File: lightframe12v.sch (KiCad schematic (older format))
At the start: 47 parts, among them J1 PJ-077, J2 Conn_01x07_Female, J4 Conn_01x07_Female, J5 Conn_01x04_Female, J6 Conn_01x4_Female, Q1 MMBT2222A-TP, Q2 MMBT2222A-TP, SW1 SW_Push, SW2 SW_Push, U1 TPS562211, U2 ESP32-WROOM-32U, U3 TLC5971

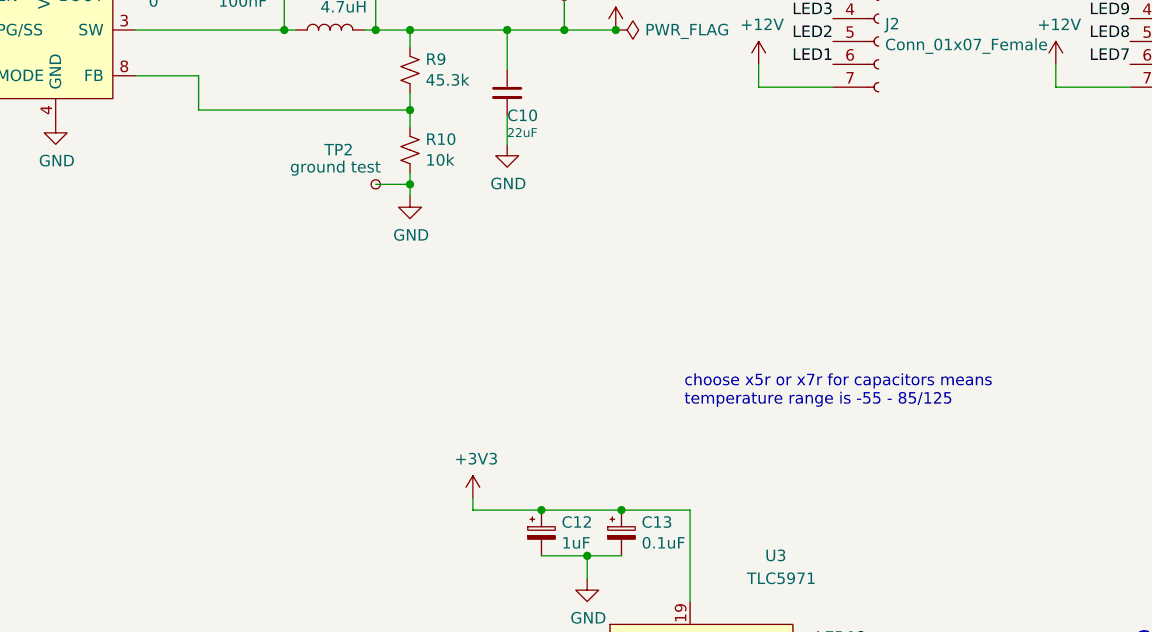
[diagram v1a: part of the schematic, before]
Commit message: Fiducials and mount points.
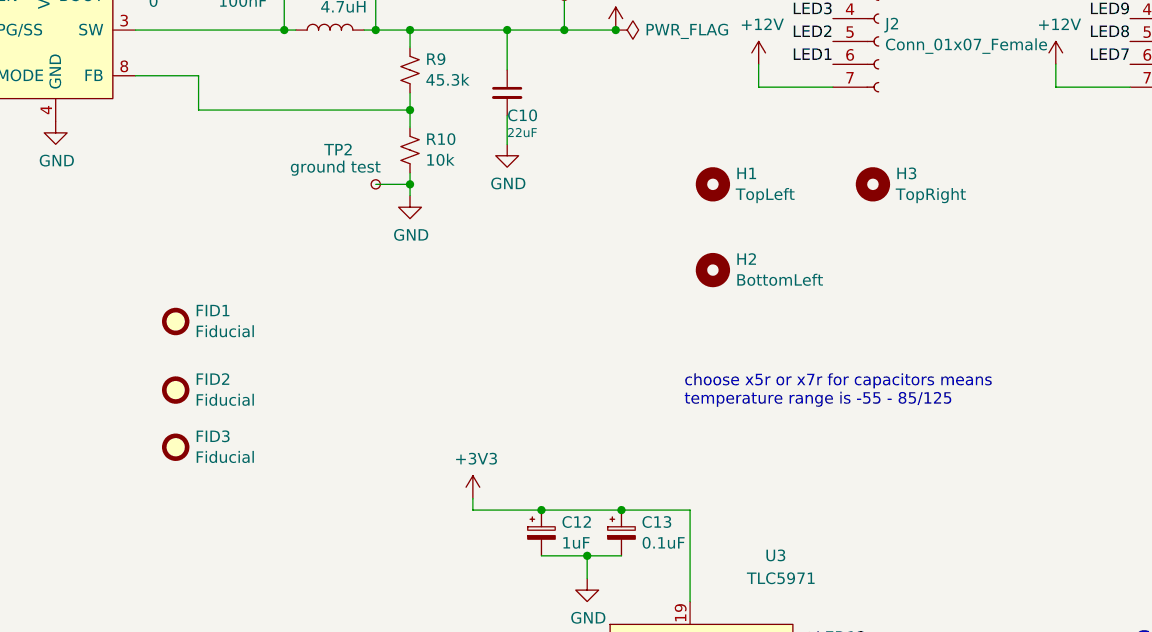
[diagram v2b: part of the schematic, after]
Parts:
- added FID1, FID2, FID3: Fiducial, Fiducial:Fiducial_1mm_Mask2mm, symbol Mechanical:Fiducial
- added H1: TopLeft, MountingHole:MountingHole_2.2mm_M2, symbol Mechanical:MountingHole
- added H2: BottomLeft, MountingHole:MountingHole_2.2mm_M2, symbol Mechanical:MountingHole
- added H3: TopRight, MountingHole:MountingHole_2.2mm_M2, symbol Mechanical:MountingHole
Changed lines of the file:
@@
+	1    0    0    -1
+$EndComp
+$Comp
+L Mechanical:MountingHole H3
+U 1 1 60715E68
+P 8550 2250
+F 0 "H3" H 8650 2296 50  0000 L CNN
+F 1 "TopRight" H 8650 2205 50  0000 L CNN
+F 2 "MountingHole:MountingHole_2.2mm_M2" H 8550 2250 50  0001 C CNN
+F 3 "~" H 8550 2250 50  0001 C CNN
+	1    8550 2250
+	1    0    0    -1
+$EndComp
+$Comp
+L Mechanical:MountingHole H1
+U 1 1 6071CBF1
+P 7850 2250
+F 0 "H1" H 7950 2296 50  0000 L CNN
+F 1 "TopLeft" H 7950 2205 50  0000 L CNN
+F 2 "MountingHole:MountingHole_2.2mm_M2" H 7850 2250 50  0001 C CNN
+F 3 "~" H 7850 2250 50  0001 C CNN
+	1    7850 2250
+	1    0    0    -1
+$EndComp
+$Comp
+L Mechanical:MountingHole H2
+U 1 1 607216A9
+P 7850 2625
+F 0 "H2" H 7950 2671 50  0000 L CNN
+F 1 "BottomLeft" H 7950 2580 50  0000 L CNN
+F 2 "MountingHole:MountingHole_2.2mm_M2" H 7850 2625 50  0001 C CNN
+F 3 "~" H 7850 2625 50  0001 C CNN
+	1    7850 2625
+	1    0    0    -1
+$EndComp
+$Comp
+L Mechanical:Fiducial FID1
+U 1 1 60726C05
+P 5500 2850
+F 0 "FID1" H 5585 2896 50  0000 L CNN
+F 1 "Fiducial" H 5585 2805 50  0000 L CNN
+F 2 "Fiducial:Fiducial_1mm_Mask2mm" H 5500 2850 50  0001 C CNN
+F 3 "~" H 5500 2850 50  0001 C CNN
+	1    5500 2850
+	1    0    0    -1
+$EndComp
+$Comp
+L Mechanical:Fiducial FID2
+U 1 1 60727705
+P 5500 3150
+F 0 "FID2" H 5585 3196 50  0000 L CNN
+F 1 "Fiducial" H 5585 3105 50  0000 L CNN
+F 2 "Fiducial:Fiducial_1mm_Mask2mm" H 5500 3150 50  0001 C CNN
+F 3 "~" H 5500 3150 50  0001 C CNN
+	1    5500 3150
+	1    0    0    -1
+$EndComp
+$Comp
+L Mechanical:Fiducial FID3
+U 1 1 6072BFCF
+P 5500 3400
+F 0 "FID3" H 5585 3446 50  0000 L CNN
+F 1 "Fiducial" H 5585 3355 50  0000 L CNN
+F 2 "Fiducial:Fiducial_1mm_Mask2mm" H 5500 3400 50  0001 C CNN
+F 3 "~" H 5500 3400 50  0001 C CNN
+	1    5500 3400
 	1    0    0    -1
 $EndComp

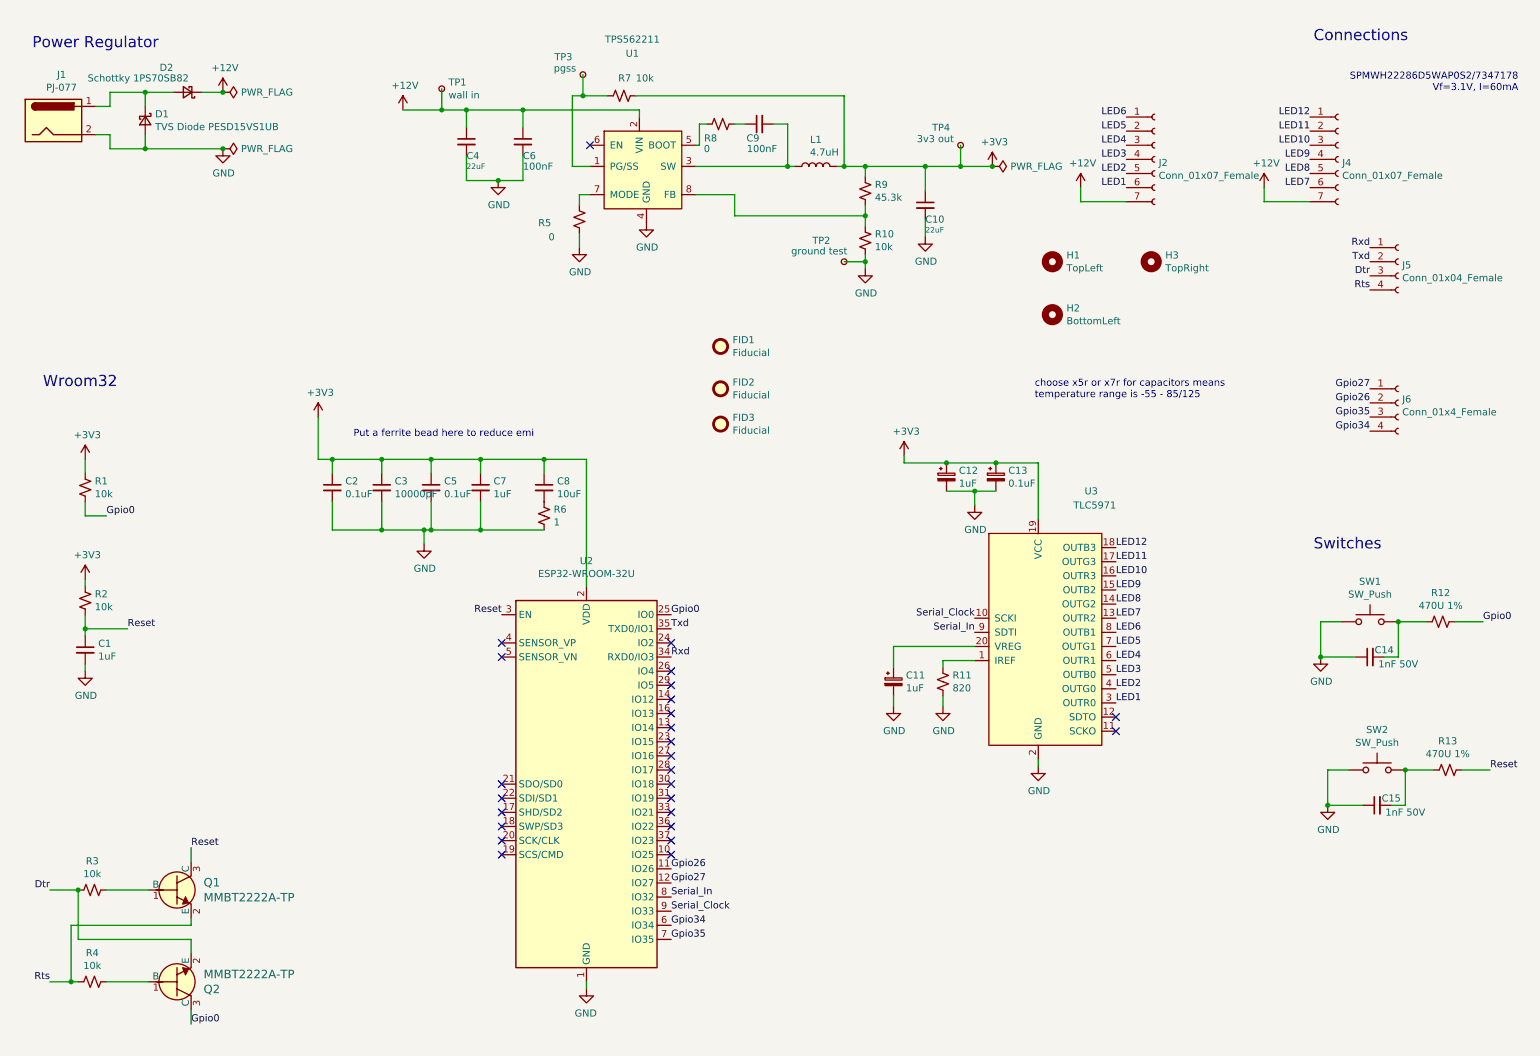
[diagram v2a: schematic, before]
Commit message: changes inductor footprint.
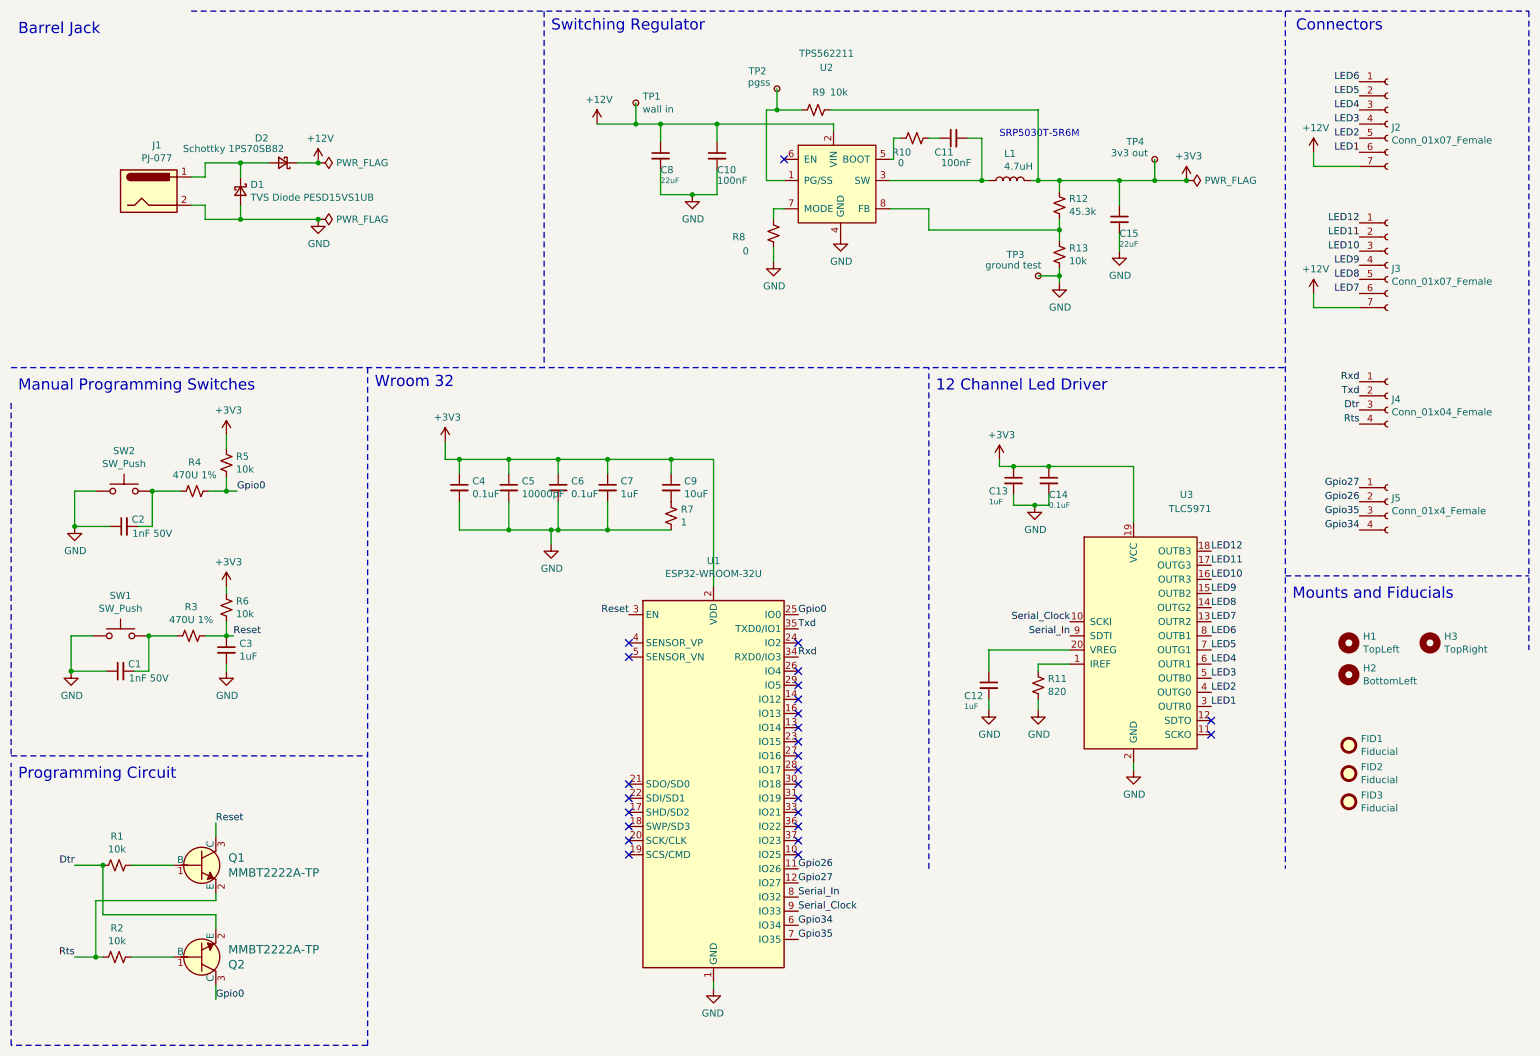
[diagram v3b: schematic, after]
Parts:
- removed C11, C12: 1uF, digikey-footprints:0603, symbol Device:CP_Small
- removed C13: 0.1uF, digikey-footprints:0603, symbol Device:CP_Small
- added C12, C13: 1uF, digikey-footprints:0603, symbol Device:C_Small
- added C14: 0.1uF, digikey-footprints:0603, symbol Device:C_Small
- L1: footprint Keith:SRN8040 Bournes -> Keith:SRP5030T-5R6M
- renumbered C15 to C1, C6 to C10, C9 to C11, C10 to C15, C14 to C2, C1 to C3, C2 to C4, C3 to C5, C5 to C6, C4 to C8, C8 to C9, J4 to J3, J5 to J4, J6 to J5, R3 to R1, R8 to R10, R9 to R12, R10 to R13, R4 to R2, R13 to R3, R12 to R4, R1 to R5, R2 to R6, R6 to R7, R5 to R8, R7 to R9, SW2 to SW1, SW1 to SW2, TP3 to TP2, TP2 to TP3, U2 to U1, U1 to U2
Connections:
- net +3V3: now also C13.1, C14.1
- net GND: now also C12.2, C13.2, C14.2
- net at U3.20 (VREG): now also C12.1
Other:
- note added: "12 Channel Led Driver"
- note added: "Barrel Jack"
- note added: "Connectors"
- note added: "Manual Programming Switches"
- note added: "Mounts and Fiducials\n"
- note added: "Programming Circuit"
- note added: "SRP5030T-5R6M"
- note added: "Switching Regulator"
- note added: "Wroom 32"
- note removed: "Connections"
- note removed: "Power Regulator"
- note removed: "Put a ferrite bead here to reduce emi"
- note removed: "SPMWH22286D5WAP0S2/7347178\nVf=3.1V, I=60mA"
- note removed: "Switches"
- note removed: "Wroom32"
- note removed: "choose x5r or x7r for capacitors means \ntemperature range is -55 - 85/125"
- moved on the sheet: C1, C10, C11, C15, C2, C3, C4, C5, C6, C7, C8, C9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

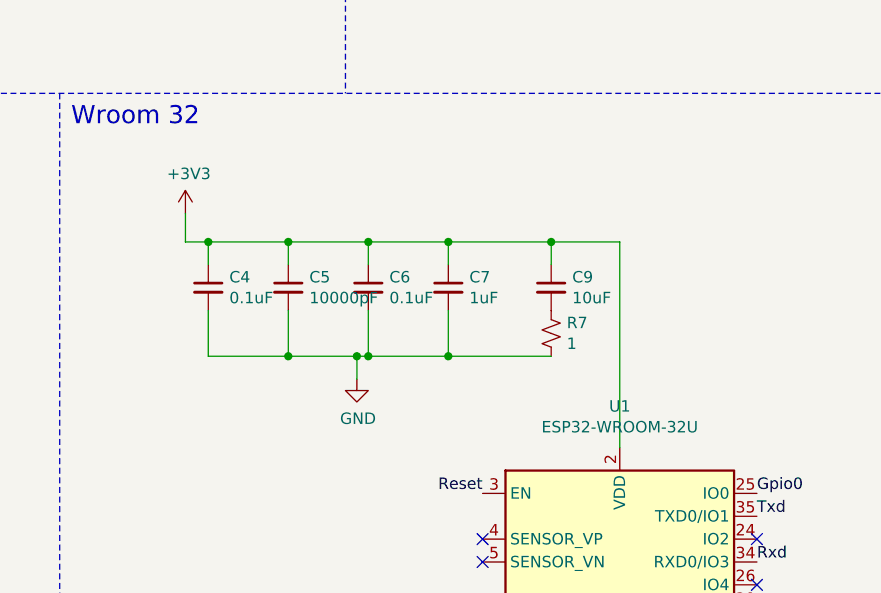
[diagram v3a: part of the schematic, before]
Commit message: Reduced decoupling and increased traces.
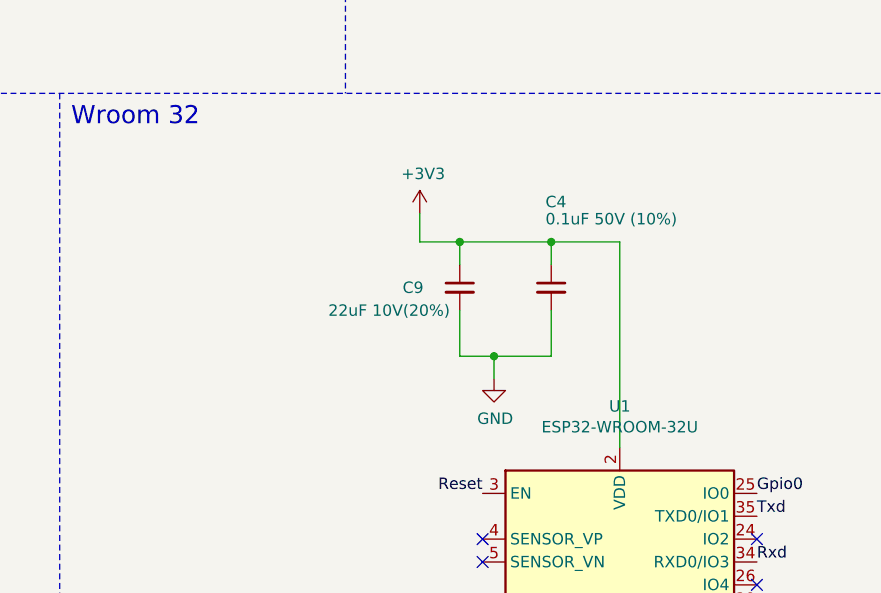
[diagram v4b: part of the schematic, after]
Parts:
- removed C5: 10000pF, digikey-footprints:0603, symbol Device:C_Small
- removed C6: 0.1uF, digikey-footprints:0603, symbol Device:C_Small
- removed C7: 1uF, digikey-footprints:0603, symbol Device:C_Small
- removed R7: 1, Resistor_SMD:R_0402_1005Metric, symbol Device:R_Small_US
- C4: value 0.1uF -> 0.1uF 50V (10%)
- C9: value 10uF -> 22uF 10V(20%)
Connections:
- net GND: now also C9.2
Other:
- moved on the sheet: C4, C9
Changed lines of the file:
@@
 NoConn ~ 6050 5150
-Wire Wire Line
-	4700 3750 4700 3650
 Wire Wire Line
 	5150 3750 5150 3650
@@
 Wire Wire Line
 	5150 3650 5450 3650
-Connection ~ 4700 3650
-Wire Wire Line
-	4700 3650 5150 3650
-Wire Wire Line
-	4350 3650 4700 3650
-Connection ~ 4350 3650
 NoConn ~ 6050 6450
 NoConn ~ 6050 6350
@@
 $EndComp
 NoConn ~ 6050 5550
-Wire Wire Line
-	4700 4150 5150 4150
-Connection ~ 4700 4150
-Wire Wire Line
-	4000 4150 4300 4150
-Connection ~ 4000 4150
-Wire Wire Line
-	3650 4150 4000 4150
-Wire Wire Line
-	4350 4150 4700 4150
 Text Label 6050 6850 0    50   ~ 0
 Serial_Clock
@@
 Text Label 4850 4750 2    50   ~ 0
 Reset
-Wire Wire Line
-	4300 4150 4350 4150
-Connection ~ 4300 4150
-Connection ~ 4350 4150
 $Comp
 L power:GND #PWR012
@@
 $EndComp
 Wire Wire Line
-	4000 3650 4350 3650
-Connection ~ 4000 3650
-Wire Wire Line
-	3650 3950 3650 4150
-$Comp
-L Device:C_Small C5
-U 1 1 60195D86
-P 4000 3850
-F 0 "C5" H 4092 3896 50  0000 L CNN
-F 1 "10000pF" H 4092 3805 50  0000 L CNN
-F 2 "digikey-footprints:0603" H 4000 3850 50  0001 C CNN
-F 3 "~" H 4000 3850 50  0001 C CNN
-	1    4000 3850
-	1    0    0    -1
-$EndComp
+	4750 3950 4750 4150
 $Comp
 L power:+3V3 #PWR08
 U 1 1 6012A417
-P 3550 3525
-F 0 "#PWR08" H 3550 3375 50  0001 C CNN
-F 1 "+3V3" H 3565 3698 50  0000 C CNN
-F 2 "" H 3550 3525 50  0001 C CNN
-F 3 "" H 3550 3525 50  0001 C CNN
-	1    3550 3525
+P 4575 3525
+F 0 "#PWR08" H 4575 3375 50  0001 C CNN
+F 1 "+3V3" H 4590 3698 50  0000 C CNN
+F 2 "" H 4575 3525 50  0001 C CNN
+F 3 "" H 4575 3525 50  0001 C CNN
+	1    4575 3525
 	1    0    0    -1
 $EndComp
@@
 L Device:C_Small C4
 U 1 1 60194547
-P 3650 3850
-F 0 "C4" H 3742 3896 50  0000 L CNN
-F 1 "0.1uF" H 3742 3805 50  0000 L CNN
-F 2 "digikey-footprints:0603" H 3650 3850 50  0001 C CNN
-F 3 "~" H 3650 3850 50  0001 C CNN
-	1    3650 3850
-	1    0    0    -1
-$EndComp
-$Comp
-L Device:C_Small C7
-U 1 1 60195102
-P 4700 3850
-F 0 "C7" H 4792 3896 50  0000 L CNN
-F 1 "1uF" H 4792 3805 50  0000 L CNN
-F 2 "digikey-footprints:0603" H 4700 3850 50  0001 C CNN
-F 3 "~" H 4700 3850 50  0001 C CNN
-	1    4700 3850
-	1    0    0    -1
-$EndComp
-$Comp
-L Device:C_Small C9
-U 1 1 60195650
 P 5150 3850
-F 0 "C9" H 5242 3896 50  0000 L CNN
-F 1 "10uF" H 5242 3805 50  0000 L CNN
-F 2 "digikey-footprints:0805" H 5150 3850 50  0001 C CNN
+F 0 "C4" H 5125 4225 50  0000 L CNN
+F 1 "0.1uF 50V (10%)" H 5125 4150 50  0000 L CNN
+F 2 "digikey-footprints:0603" H 5150 3850 50  0001 C CNN
 F 3 "~" H 5150 3850 50  0001 C CNN
 	1    5150 3850
 	1    0    0    -1
 $EndComp
-$Comp
-L Device:R_Small_US R7
-U 1 1 601AF3F3
-P 5150 4050
-F 0 "R7" H 5218 4096 50  0000 L CNN
-F 1 "1" H 5218 4005 50  0000 L CNN
-F 2 "Resistor_SMD:R_0402_1005Metric" H 5150 4050 50  0001 C CNN
-F 3 "~" H 5150 4050 50  0001 C CNN
-	1    5150 4050
-	1    0    0    -1
-$EndComp
-Wire Wire Line
-	4000 3950 4000 4150
-Wire Wire Line
-	4700 3950 4700 4150
-Wire Wire Line
-	4300 4150 4300 4250
+Wire Wire Line
+	4900 4150 4900 4250
 $Comp
 L power:GND #PWR09
 U 1 1 601C0C19
-P 4300 4250
-F 0 "#PWR09" H 4300 4000 50  0001 C CNN
-F 1 "GND" H 4305 4077 50  0000 C CNN
-F 2 "" H 4300 4250 50  0001 C CNN
-F 3 "" H 4300 4250 50  0001 C CNN
-	1    4300 4250
-	1    0    0    -1
-$EndComp
-Wire Wire Line
-	4350 3950 4350 4150
-$Comp
-L Device:C_Small C6
-U 1 1 60267B17
-P 4350 3850
-F 0 "C6" H 4442 3896 50  0000 L CNN
-F 1 "0.1uF" H 4442 3805 50  0000 L CNN
-F 2 "digikey-footprints:0603" H 4350 3850 50  0001 C CNN
-F 3 "~" H 4350 3850 50  0001 C CNN
-	1    4350 3850
-	1    0    0    -1
-$EndComp
-Wire Wire Line
-	4350 3750 4350 3650
-Wire Wire Line
-	4000 3750 4000 3650
-Wire Wire Line
-	3650 3750 3650 3650
-Wire Wire Line
-	3550 3650 3650 3650
-Connection ~ 3650 3650
-Wire Wire Line
-	3650 3650 4000 3650
+P 4900 4250
+F 0 "#PWR09" H 4900 4000 50  0001 C CNN
+F 1 "GND" H 4905 4077 50  0000 C CNN
+F 2 "" H 4900 4250 50  0001 C CNN
+F 3 "" H 4900 4250 50  0001 C CNN
+	1    4900 4250
+	1    0    0    -1
+$EndComp
 Text Notes 7025 3175 0    79   ~ 0
 12 Channel Led Driver
@@
 Wroom 32
 Wire Wire Line
-	3550 3650 3550 3525
+	4575 3650 4575 3525
 Wire Notes Line
 	3000 3000 3000 7800
@@
 	1    0    0    -1
 $EndComp
+Wire Wire Line
+	4750 3650 5150 3650
+Wire Wire Line
+	4750 4150 4900 4150
+Connection ~ 4900 4150
+Wire Wire Line
+	4900 4150 5150 4150
+Wire Wire Line
+	4750 3650 4575 3650
+Connection ~ 4750 3650
+Wire Wire Line
+	4750 3750 4750 3650
+$Comp
+L Device:C_Small C9
+U 1 1 60195650
+P 4750 3850
+F 0 "C9" H 4500 3850 50  0000 L CNN
+F 1 "22uF 10V(20%)" H 4175 3750 50  0000 L CNN
+F 2 "digikey-footprints:0805" H 4750 3850 50  0001 C CNN
+F 3 "~" H 4750 3850 50  0001 C CNN
+	1    4750 3850
+	1    0    0    -1
+$EndComp
+Wire Wire Line
+	5150 3950 5150 4150
 $EndSCHEMATC
